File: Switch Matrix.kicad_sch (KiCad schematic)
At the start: 131 parts, among them SW1 SD_6B1D, SW10 SD_4B1E, SW100 SD_4B3E, SW101 SD_4B3E, SW102 SD_4B3E, SW103 SD_4B3E, SW104 SD_4B3E, SW105 SD_4B3E, SW106 SD_4B3E, SW107 SD_4B3E, SW108 SD_4B3E, SW109 SD_4B3E, SW11 SD_4B1E, SW110 SD_4B3E, SW111 SD_4B3E, SW112 SD_6B1D, SW113 SD_4B3E, SW114 SD_4B3E, SW115 UNPOPULATED, SW116 SD_4B3E, SW117 SD_5B3E, SW118 SD_4B3E, SW119 UNPOPULATED, SW12 SD_6B1D, SW120 SD_4B3E, SW121 SD_4B3E, SW122 SD_4B3E, SW122a0 UNPOPULATED, SW123 SD_4B3E, SW123a0 UNPOPULATED, SW124 UNPOPULATED, SW124a0 SD_4B3E, SW125 SD_4B3E, SW126 SD_4B3E, SW127 UNPOPULATED, SW128 SD_4B3E, SW13 SD_4B1E, SW14 SD_6B1D, SW15 SD_4B1E, SW16 SD_6B1D, SW17 SD_4B1E, SW18 SD_6B1D, SW19 SD_4B1E, SW2 SD_4B1E, SW20 SD_6B1D, SW21 SD_4B1E, SW22 SD_6B1D, SW23 SD_4B1E, SW24 SD_6B1D, SW25 SD_4B3E, SW26 SD_4B3E, SW27 SD_6B1D, SW28 SD_4B3E, SW29 SD_4B3E, SW3 SD_6B1D, SW30 SD_4B3E, SW31 SD_4B3E, SW32 SD_4B3E, SW33 SD_4B3E, SW34 SD_4B3E, SW35 SD_4B3E, SW36 SD_4B3E, SW37 SD_4B3E, SW38 SD_4B3E, SW39 SD_4B3E, SW4 SD_4B1E, SW40 SD_4B3E, SW41 UNPOPULATED, SW42 SD_4B3E, SW43 SD_4B3E, SW44 SD_4B3E, SW45 SD_4B3E, SW46 SD_6B1D, SW47 SD_4B3E, SW48 SD_4B3E, SW49 SD_4B3E, SW5 SD_6B1D, SW50 SD_4B3E, SW51 SD_4B3E, SW52 SD_6B1D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

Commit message: wip: remove +5v line
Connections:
- removed net +5V: SW1.2 (+5V), SW10.2 (+5V), SW100.2 (+5V), SW101.2 (+5V), SW102.2 (+5V), SW103.2 (+5V), SW104.2 (+5V), SW105.2 (+5V), SW106.2 (+5V), SW107.2 (+5V), SW108.2 (+5V), SW109.2 (+5V), SW11.2 (+5V), SW110.2 (+5V), SW111.2 (+5V), SW112.2 (+5V), SW113.2 (+5V), SW114.2 (+5V), SW115.2 (+5V), SW116.2 (+5V), SW117.2 (+5V), SW118.2 (+5V), SW119.2 (+5V), SW12.2 (+5V), SW120.2 (+5V), SW121.2 (+5V), SW122.2 (+5V), SW122a0.2 (+5V), SW123.2 (+5V), SW123a0.2 (+5V), SW124.2 (+5V), SW124a0.2 (+5V), SW125.2 (+5V), SW126.2 (+5V), SW127.2 (+5V), SW128.2 (+5V), SW13.2 (+5V), SW14.2 (+5V), SW15.2 (+5V), SW16.2 (+5V), SW17.2 (+5V), SW18.2 (+5V), SW19.2 (+5V), SW2.2 (+5V), SW20.2 (+5V), SW21.2 (+5V), SW22.2 (+5V), SW23.2 (+5V), SW24.2 (+5V), SW25.2 (+5V), SW26.2 (+5V), SW27.2 (+5V), SW28.2 (+5V), SW29.2 (+5V), SW3.2 (+5V), SW30.2 (+5V), SW31.2 (+5V), SW32.2 (+5V), SW33.2 (+5V), SW34.2 (+5V), SW35.2 (+5V), SW36.2 (+5V), SW37.2 (+5V), SW38.2 (+5V), SW39.2 (+5V), SW4.2 (+5V), SW40.2 (+5V), SW41.2 (+5V), SW42.2 (+5V), SW43.2 (+5V), SW44.2 (+5V), SW45.2 (+5V), SW46.2 (+5V), SW47.2 (+5V), SW48.2 (+5V), SW49.2 (+5V), SW5.2 (+5V), SW50.2 (+5V), SW51.2 (+5V), SW52.2 (+5V), SW53.2 (+5V), SW54.2 (+5V), SW55.2 (+5V), SW56.2 (+5V), SW57.2 (+5V), SW58.2 (+5V), SW59.2 (+5V), SW6.2 (+5V), SW60.2 (+5V), SW61.2 (+5V), SW62.2 (+5V), SW63.2 (+5V), SW64.2 (+5V), SW65.2 (+5V), SW66.2 (+5V), SW67.2 (+5V), SW68.2 (+5V), SW69.2 (+5V), SW7.2 (+5V), SW70.2 (+5V), SW71.2 (+5V), SW72.2 (+5V), SW73.2 (+5V), SW74.2 (+5V), SW75.2 (+5V), SW76.2 (+5V), SW77.2 (+5V), SW78.2 (+5V), SW79.2 (+5V), SW8.2 (+5V), SW80.2 (+5V), SW81.2 (+5V), SW82.2 (+5V), SW83.2 (+5V), SW84.2 (+5V), SW85.2 (+5V), SW86.2 (+5V), SW87.2 (+5V), SW88.2 (+5V), SW89.2 (+5V), SW9.2 (+5V), SW90.2 (+5V), SW91.2 (+5V), SW92.2 (+5V), SW93.2 (+5V), SW94.2 (+5V), SW95.2 (+5V), SW96.2 (+5V), SW97.2 (+5V), SW98.2 (+5V), SW99.2 (+5V)

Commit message: wip: footprint and symbols update 1
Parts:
- SW1, SW10, SW100, SW101, SW102, SW103, SW104, SW105, SW106, SW107, SW108, SW109, SW11, SW110, SW111, SW112, SW113, SW114, SW115, SW116, SW117, SW118, SW119, SW12, SW120, SW121, SW122, SW122a0, SW123, SW123a0, SW124, SW124a0, SW125, SW126, SW127, SW128, SW13, SW14, SW15, SW16, SW17, SW18, SW19, SW2, SW20, SW21, SW22, SW23, SW24, SW25, SW26, SW27, SW28, SW29, SW3, SW30, SW31, SW32, SW33, SW34, SW35, SW36, SW37, SW38, SW39, SW4, SW40, SW41, SW42, SW43, SW44, SW45, SW46, SW47, SW48, SW49, SW5, SW50, SW51, SW52, SW53, SW54, SW55, SW56, SW57, SW58, SW59, SW6, SW60, SW61, SW62, SW63, SW64, SW65, SW66, SW67, SW68, SW69, SW7, SW70, SW71, SW72, SW73, SW74, SW75, SW76, SW77, SW78, SW79, SW8, SW80, SW81, SW82, SW83, SW84, SW85, SW86, SW87, SW88, SW89, SW9, SW90, SW91, SW92, SW93, SW94, SW95, SW96, SW97, SW98, SW99: symbol MicroSwitch_SD_4B3E:SD_4B3E -> MicroSwitch:MicroSwitchSDSeriesE

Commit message: pcb diode 1,2 row placement
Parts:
- added D1, D10, D100, D101, D102, D103, D104, D105, D106, D107, D108, D109, D11, D110, D111, D112, D113, D114, D115, D116, D117, D118, D119, D12, D120, D122, D123, D124, D125, D126, D127, D128, D13, D14, D15, D16, D17, D18, D19, D2, D20, D21, D22, D23, D24, D25, D26, D27, D28, D29, D3, D30, D31, D32, D33, D34, D35, D36, D37, D38, D39, D4, D40, D41, D42, D43, D44, D45, D46, D47, D48, D49, D5, D50, D51, D52, D53, D54, D55, D56, D57, D58, D59, D6, D60, D61, D62, D63, D64, D65, D66, D67, D68, D69, D7, D70, D71, D72, D73, D74, D75, D76, D77, D78, D79, D8, D80, D81, D82, D83, D84, D85, D86, D87, D88, D89, D9, D90, D91, D92, D93, D94, D95, D96, D97, D98, D99, D`1`17: D, Diode_THT:D_A-405_P7.62mm_Horizontal, symbol Device:D
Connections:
- net COL0: now also SW120.1 (in), SW22.1 (in), SW26.1 (in), SW3.1 (in), SW46.1 (in), SW50.1 (in), SW73.1 (in), SW97.1 (in); no longer SW120.3 (VOUT), SW22.3 (VOUT), SW26.3 (VOUT), SW3.3 (VOUT), SW46.3 (VOUT), SW50.3 (VOUT), SW73.3 (VOUT), SW97.3 (VOUT)
- net COL1: now also SW119.1 (in), SW2.1 (in), SW23.1 (in), SW25.1 (in), SW47.1 (in), SW49.1 (in), SW72.1 (in), SW96.1 (in); no longer SW119.3 (VOUT), SW2.3 (VOUT), SW23.3 (VOUT), SW25.3 (VOUT), SW47.3 (VOUT), SW49.3 (VOUT), SW72.3 (VOUT), SW96.3 (VOUT)
- net COL10: now also SW106.1 (in), SW11.1 (in), SW115.1 (in), SW35.1 (in), SW59.1 (in), SW69.1 (in), SW82.1 (in), SW92.1 (in); no longer SW106.3 (VOUT), SW11.3 (VOUT), SW115.3 (VOUT), SW35.3 (VOUT), SW59.3 (VOUT), SW69.3 (VOUT), SW82.3 (VOUT), SW92.3 (VOUT)
- net COL11: now also SW107.1 (in), SW114.1 (in), SW12.1 (in), SW36.1 (in), SW60.1 (in), SW68.1 (in), SW83.1 (in), SW91.1 (in); no longer SW107.3 (VOUT), SW114.3 (VOUT), SW12.3 (VOUT), SW36.3 (VOUT), SW60.3 (VOUT), SW68.3 (VOUT), SW83.3 (VOUT), SW91.3 (VOUT)
- net COL12: now also SW108.1 (in), SW113.1 (in), SW13.1 (in), SW37.1 (in), SW61.1 (in), SW67.1 (in), SW84.1 (in), SW90.1 (in); no longer SW108.3 (VOUT), SW113.3 (VOUT), SW13.3 (VOUT), SW37.3 (VOUT), SW61.3 (VOUT), SW67.3 (VOUT), SW84.3 (VOUT), SW90.3 (VOUT)
- net COL13: now also SW123.1 (in), SW123a0.1 (in), SW127.1 (in), SW16.1 (in), SW40.1 (in), SW64.1 (in), SW65.1 (in), SW87.1 (in), SW88.1 (in); no longer SW123.3 (VOUT), SW123a0.3 (VOUT), SW127.3 (VOUT), SW16.3 (VOUT), SW40.3 (VOUT), SW64.3 (VOUT), SW65.3 (VOUT), SW87.3 (VOUT), SW88.3 (VOUT)
- net COL14: now also SW109.1 (in), SW112.1 (in), SW14.1 (in), SW38.1 (in), SW62.1 (in), SW66.1 (in), SW85.1 (in), SW89.1 (in); no longer SW109.3 (VOUT), SW112.3 (VOUT), SW14.3 (VOUT), SW38.3 (VOUT), SW62.3 (VOUT), SW66.3 (VOUT), SW85.3 (VOUT), SW89.3 (VOUT)
- net COL15: now also SW110.1 (in), SW128.1 (in), SW15.1 (in), SW24.1 (in), SW39.1 (in), SW48.1 (in), SW63.1 (in), SW86.1 (in); no longer SW110.3 (VOUT), SW128.3 (VOUT), SW15.3 (VOUT), SW24.3 (VOUT), SW39.3 (VOUT), SW48.3 (VOUT), SW63.3 (VOUT), SW86.3 (VOUT)
- net COL2: now also SW121.1 (in), SW21.1 (in), SW27.1 (in), SW4.1 (in), SW45.1 (in), SW51.1 (in), SW74.1 (in), SW98.1 (in); no longer SW121.3 (VOUT), SW21.3 (VOUT), SW27.3 (VOUT), SW4.3 (VOUT), SW45.3 (VOUT), SW51.3 (VOUT), SW74.3 (VOUT), SW98.3 (VOUT)
- net COL3: now also SW118.1 (in), SW20.1 (in), SW28.1 (in), SW44.1 (in), SW5.1 (in), SW52.1 (in), SW75.1 (in), SW99.1 (in); no longer SW118.3 (VOUT), SW20.3 (VOUT), SW28.3 (VOUT), SW44.3 (VOUT), SW5.3 (VOUT), SW52.3 (VOUT), SW75.3 (VOUT), SW99.3 (VOUT)
- net COL4: now also SW1.1 (in), SW100.1 (in), SW111.1 (in), SW122.1 (in), SW122a0.1 (in), SW124.1 (in), SW124a0.1 (in), SW29.1 (in), SW53.1 (in), SW76.1 (in); no longer SW1.3 (VOUT), SW100.3 (VOUT), SW111.3 (VOUT), SW122.3 (VOUT), SW122a0.3 (VOUT), SW124.3 (VOUT), SW124a0.3 (VOUT), SW29.3 (VOUT), SW53.3 (VOUT), SW76.3 (VOUT)
- net COL5: now also SW101.1 (in), SW18.1 (in), SW30.1 (in), SW42.1 (in), SW54.1 (in), SW6.1 (in), SW77.1 (in), SW95.1 (in); no longer SW101.3 (VOUT), SW18.3 (VOUT), SW30.3 (VOUT), SW42.3 (VOUT), SW54.3 (VOUT), SW6.3 (VOUT), SW77.3 (VOUT), SW95.3 (VOUT)
- net COL6: now also SW102.1 (in), SW126.1 (in), SW17.1 (in), SW31.1 (in), SW41.1 (in), SW55.1 (in), SW7.1 (in), SW78.1 (in); no longer SW102.3 (VOUT), SW126.3 (VOUT), SW17.3 (VOUT), SW31.3 (VOUT), SW41.3 (VOUT), SW55.3 (VOUT), SW7.3 (VOUT), SW78.3 (VOUT)
- net COL7: now also SW103.1 (in), SW125.1 (in), SW19.1 (in), SW32.1 (in), SW43.1 (in), SW56.1 (in), SW79.1 (in), SW8.1 (in); no longer SW103.3 (VOUT), SW125.3 (VOUT), SW19.3 (VOUT), SW32.3 (VOUT), SW43.3 (VOUT), SW56.3 (VOUT), SW79.3 (VOUT), SW8.3 (VOUT)
- net COL8: now also SW104.1 (in), SW117.1 (in), SW33.1 (in), SW57.1 (in), SW71.1 (in), SW80.1 (in), SW9.1 (in), SW94.1 (in); no longer SW104.3 (VOUT), SW117.3 (VOUT), SW33.3 (VOUT), SW57.3 (VOUT), SW71.3 (VOUT), SW80.3 (VOUT), SW9.3 (VOUT), SW94.3 (VOUT)
- net COL9: now also SW10.1 (in), SW105.1 (in), SW116.1 (in), SW34.1 (in), SW58.1 (in), SW70.1 (in), SW81.1 (in), SW93.1 (in); no longer SW10.3 (VOUT), SW105.3 (VOUT), SW116.3 (VOUT), SW34.3 (VOUT), SW58.3 (VOUT), SW70.3 (VOUT), SW81.3 (VOUT), SW93.3 (VOUT)
- net ROW0: now also SW122a0.2 (out); no longer SW10.1 (VCC), SW11.1 (VCC), SW12.1 (VCC), SW122.1 (VCC), SW122a0.1 (VCC), SW13.1 (VCC), SW14.1 (VCC), SW15.1 (VCC), SW16.1 (VCC), SW2.1 (VCC), SW3.1 (VCC), SW4.1 (VCC), SW5.1 (VCC), SW6.1 (VCC), SW7.1 (VCC), SW8.1 (VCC), SW9.1 (VCC)
- net ROW1: now also D25.1 (K), D26.1 (K), D27.1 (K), D28.1 (K), D29.1 (K), D30.1 (K), D31.1 (K), D32.1 (K), D33.1 (K), D34.1 (K), D35.1 (K), D36.1 (K), D37.1 (K), D38.1 (K), D39.1 (K), D40.1 (K); no longer SW25.1 (VCC), SW26.1 (VCC), SW27.1 (VCC), SW28.1 (VCC), SW29.1 (VCC), SW30.1 (VCC), SW31.1 (VCC), SW32.1 (VCC), SW33.1 (VCC), SW34.1 (VCC), SW35.1 (VCC), SW36.1 (VCC), SW37.1 (VCC), SW38.1 (VCC), SW39.1 (VCC), SW40.1 (VCC)
- net ROW2: now also D49.1 (K), D50.1 (K), D51.1 (K), D52.1 (K), D53.1 (K), D54.1 (K), D55.1 (K), D56.1 (K); no longer SW49.1 (VCC), SW50.1 (VCC), SW51.1 (VCC), SW52.1 (VCC), SW53.1 (VCC), SW54.1 (VCC), SW55.1 (VCC), SW56.1 (VCC), SW57.1 (VCC), SW58.1 (VCC), SW59.1 (VCC), SW60.1 (VCC), SW61.1 (VCC), SW62.1 (VCC), SW63.1 (VCC), SW64.1 (VCC)
- net ROW3: now also D72.1 (K), D73.1 (K), D74.1 (K), D75.1 (K), D76.1 (K), D77.1 (K), D78.1 (K), D79.1 (K); no longer SW72.1 (VCC), SW73.1 (VCC), SW74.1 (VCC), SW75.1 (VCC), SW76.1 (VCC), SW77.1 (VCC), SW78.1 (VCC), SW79.1 (VCC), SW80.1 (VCC), SW81.1 (VCC), SW82.1 (VCC), SW83.1 (VCC), SW84.1 (VCC), SW85.1 (VCC), SW86.1 (VCC), SW87.1 (VCC)
- net ROW4: now also SW123a0.2 (out), D100.1 (K), D101.1 (K), D102.1 (K), D103.1 (K), D96.1 (K), D97.1 (K), D98.1 (K), D99.1 (K); no longer SW100.1 (VCC), SW101.1 (VCC), SW102.1 (VCC), SW103.1 (VCC), SW104.1 (VCC), SW105.1 (VCC), SW106.1 (VCC), SW107.1 (VCC), SW108.1 (VCC), SW109.1 (VCC), SW110.1 (VCC), SW123.1 (VCC), SW123a0.1 (VCC), SW96.1 (VCC), SW97.1 (VCC), SW98.1 (VCC), SW99.1 (VCC)
- net ROW5: now also D111.1 (K), D118.1 (K), D119.1 (K), D120.1 (K), D125.1 (K), D126.1 (K), D95.1 (K), D`1`17.1 (K); no longer SW111.1 (VCC), SW112.1 (VCC), SW113.1 (VCC), SW114.1 (VCC), SW115.1 (VCC), SW116.1 (VCC), SW117.1 (VCC), SW118.1 (VCC), SW119.1 (VCC), SW120.1 (VCC), SW121.1 (VCC), SW125.1 (VCC), SW126.1 (VCC), SW127.1 (VCC), SW128.1 (VCC), SW95.1 (VCC)
- net ROW6: now also SW124a0.2 (out), D1.1 (K), D124.1 (K), D17.1 (K), D18.1 (K), D19.1 (K), D20.1 (K), D21.1 (K), D22.1 (K), D23.1 (K), D41.1 (K), D42.1 (K), D43.1 (K), D44.1 (K), D45.1 (K), D46.1 (K), D47.1 (K); no longer SW124.1 (VCC), SW124a0.1 (VCC), SW41.1 (VCC), SW42.1 (VCC), SW43.1 (VCC), SW44.1 (VCC), SW45.1 (VCC), SW46.1 (VCC), SW47.1 (VCC), SW48.1 (VCC), SW88.1 (VCC), SW89.1 (VCC), SW90.1 (VCC), SW91.1 (VCC), SW92.1 (VCC), SW93.1 (VCC), SW94.1 (VCC)
- removed net ROW7: SW1.1 (VCC), SW17.1 (VCC), SW18.1 (VCC), SW19.1 (VCC), SW20.1 (VCC), SW21.1 (VCC), SW22.1 (VCC), SW23.1 (VCC), SW24.1 (VCC), SW65.1 (VCC), SW66.1 (VCC), SW67.1 (VCC), SW68.1 (VCC), SW69.1 (VCC), SW70.1 (VCC), SW71.1 (VCC)
- new net: D80.1 (K), D81.1 (K), D82.1 (K), D83.1 (K), D84.1 (K), D85.1 (K), D86.1 (K), D87.1 (K)
- new net: D85.2 (A), SW85.2 (out)
- new net: D48.2 (A), SW48.2 (out)
- new net: D41.2 (A), SW41.2 (out)
- new net: D123.2 (A), SW123.2 (out)
- new net: D4.2 (A), SW4.2 (out)
- new net: D57.1 (K), D58.1 (K), D59.1 (K), D60.1 (K), D61.1 (K), D62.1 (K), D63.1 (K), D64.1 (K)
- new net: D58.2 (A), SW58.2 (out)
- new net: D104.1 (K), D105.1 (K), D106.1 (K), D107.1 (K), D108.1 (K), D109.1 (K), D110.1 (K), D123.1 (K)
- new net: D109.2 (A), SW109.2 (out)
- new net: D119.2 (A), SW119.2 (out)
- new net: D11.2 (A), SW11.2 (out)
- new net: D21.2 (A), SW21.2 (out)
- new net: D29.2 (A), SW29.2 (out)
- new net: D24.1 (K), D65.1 (K), D66.1 (K), D67.1 (K), D68.1 (K), D69.1 (K), D70.1 (K), D71.1 (K)
- new net: D68.2 (A), SW68.2 (out)
- new net: D18.2 (A), SW18.2 (out)
- new net: D98.2 (A), SW98.2 (out)
- new net: D90.2 (A), SW90.2 (out)
- new net: D89.2 (A), SW89.2 (out)
- new net: D84.2 (A), SW84.2 (out)
- new net: D112.1 (K), D113.1 (K), D114.1 (K), D115.1 (K), D116.1 (K), D117.1 (K), D127.1 (K), D128.1 (K)
- new net: D114.2 (A), SW114.2 (out)
- new net: D117.2 (A), SW117.2 (out)
- new net: D36.2 (A), SW36.2 (out)
- new net: D111.2 (A), SW111.2 (out)
- new net: D10.1 (K), D11.1 (K), D122.1 (K), D2.1 (K), D3.1 (K), D4.1 (K), D5.1 (K), D6.1 (K), D7.1 (K), D8.1 (K), D9.1 (K)
- new net: D3.2 (A), SW3.2 (out)
- new net: D124.2 (A), SW124.2 (out)
- new net: D106.2 (A), SW106.2 (out)
- new net: D120.2 (A), SW120.2 (out)
- new net: D70.2 (A), SW70.2 (out)
- new net: D80.2 (A), SW80.2 (out)
- new net: D128.2 (A), SW128.2 (out)
- new net: D45.2 (A), SW45.2 (out)
- new net: D97.2 (A), SW97.2 (out)
- new net: D107.2 (A), SW107.2 (out)
- new net: D15.2 (A), SW15.2 (out)
- new net: D71.2 (A), SW71.2 (out)
- new net: D118.2 (A), SW118.2 (out)
- new net: D108.2 (A), SW108.2 (out)
- new net: D99.2 (A), SW99.2 (out)
- new net: D51.2 (A), SW51.2 (out)
- new net: D1.2 (A), SW1.2 (out)
- new net: D83.2 (A), SW83.2 (out)
- new net: D86.2 (A), SW86.2 (out)
- new net: D12.1 (K), D13.1 (K), D14.1 (K), D15.1 (K), D16.1 (K)
- new net: D52.2 (A), SW52.2 (out)
- new net: D110.2 (A), SW110.2 (out)
- new net: D66.2 (A), SW66.2 (out)
- new net: D77.2 (A), SW77.2 (out)
- new net: D59.2 (A), SW59.2 (out)
- new net: D54.2 (A), SW54.2 (out)
- new net: D6.2 (A), SW6.2 (out)
- new net: D24.2 (A), SW24.2 (out)
- new net: D43.2 (A), SW43.2 (out)
- new net: D47.2 (A), SW47.2 (out)
- new net: D61.2 (A), SW61.2 (out)
- new net: D96.2 (A), SW96.2 (out)
- new net: D63.2 (A), SW63.2 (out)
- new net: D125.2 (A), SW125.2 (out)
- new net: D46.2 (A), SW46.2 (out)
- new net: D32.2 (A), SW32.2 (out)
- new net: D53.2 (A), SW53.2 (out)
- new net: D34.2 (A), SW34.2 (out)
- new net: D39.2 (A), SW39.2 (out)
- new net: D79.2 (A), SW79.2 (out)
- new net: D115.2 (A), SW115.2 (out)
- new net: D102.2 (A), SW102.2 (out)
- new net: D9.2 (A), SW9.2 (out)
- new net: D5.2 (A), SW5.2 (out)
- new net: D94.2 (A), SW94.2 (out)
- new net: D26.2 (A), SW26.2 (out)
- new net: D104.2 (A), SW104.2 (out)
- new net: D69.2 (A), SW69.2 (out)
- new net: D73.2 (A), SW73.2 (out)
- new net: D22.2 (A), SW22.2 (out)
- new net: D95.2 (A), SW95.2 (out)
- new net: D48.1 (K), D88.1 (K), D89.1 (K), D90.1 (K), D91.1 (K), D92.1 (K), D93.1 (K), D94.1 (K)
- new net: D57.2 (A), SW57.2 (out)
- new net: D40.2 (A), SW40.2 (out)
- new net: D72.2 (A), SW72.2 (out)
- new net: D65.2 (A), SW65.2 (out)
- new net: D81.2 (A), SW81.2 (out)
- new net: D64.2 (A), SW64.2 (out)
- new net: D100.2 (A), SW100.2 (out)
- new net: D28.2 (A), SW28.2 (out)
- new net: D37.2 (A), SW37.2 (out)
- new net: D74.2 (A), SW74.2 (out)
- new net: D60.2 (A), SW60.2 (out)
- new net: D103.2 (A), SW103.2 (out)
- new net: D10.2 (A), SW10.2 (out)
- new net: D105.2 (A), SW105.2 (out)
- new net: D56.2 (A), SW56.2 (out)
- new net: D75.2 (A), SW75.2 (out)
- new net: D88.2 (A), SW88.2 (out)
- new net: D67.2 (A), SW67.2 (out)
- new net: D122.2 (A), SW122.2 (out)
- new net: D19.2 (A), SW19.2 (out)
- new net: D101.2 (A), SW101.2 (out)
- new net: D50.2 (A), SW50.2 (out)
- new net: D112.2 (A), SW112.2 (out)
- new net: D13.2 (A), SW13.2 (out)
- new net: D87.2 (A), SW87.2 (out)
- new net: D44.2 (A), SW44.2 (out)
- new net: D27.2 (A), SW27.2 (out)
- new net: D127.2 (A), SW127.2 (out)
- new net: D62.2 (A), SW62.2 (out)
- new net: D38.2 (A), SW38.2 (out)
- new net: D116.2 (A), SW116.2 (out)
- new net: D31.2 (A), SW31.2 (out)
- new net: D16.2 (A), SW16.2 (out)
- new net: D82.2 (A), SW82.2 (out)
- new net: D55.2 (A), SW55.2 (out)
- new net: D30.2 (A), SW30.2 (out)
- new net: D`1`17.2 (A), SW121.2 (out)
- new net: D14.2 (A), SW14.2 (out)
- new net: D49.2 (A), SW49.2 (out)
- new net: D93.2 (A), SW93.2 (out)
- new net: D91.2 (A), SW91.2 (out)
- new net: D78.2 (A), SW78.2 (out)
- new net: D76.2 (A), SW76.2 (out)
- new net: D113.2 (A), SW113.2 (out)
- new net: D7.2 (A), SW7.2 (out)
- new net: D33.2 (A), SW33.2 (out)
- new net: D42.2 (A), SW42.2 (out)
- new net: D12.2 (A), SW12.2 (out)
- new net: D23.2 (A), SW23.2 (out)
- new net: D35.2 (A), SW35.2 (out)
- new net: D92.2 (A), SW92.2 (out)
- new net: D17.2 (A), SW17.2 (out)
- new net: D25.2 (A), SW25.2 (out)
- new net: D8.2 (A), SW8.2 (out)
- new net: D126.2 (A), SW126.2 (out)
- new net: D2.2 (A), SW2.2 (out)
- new net: D20.2 (A), SW20.2 (out)
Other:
- moved on the sheet: SW1, SW10, SW100, SW101, SW102, SW103, SW104, SW105, SW106, SW107, SW108, SW109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

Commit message: wip: pcb tuning
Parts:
- D1, D10, D100, D101, D102, D103, D104, D105, D106, D107, D108, D109, D11, D110, D111, D112, D113, D114, D115, D116, D117, D118, D119, D12, D120, D122, D123, D124, D125, D126, D127, D128, D13, D14, D15, D16, D17, D18, D19, D2, D20, D21, D22, D23, D24, D25, D26, D27, D28, D29, D3, D30, D31, D32, D33, D34, D35, D36, D37, D38, D39, D4, D40, D41, D42, D43, D44, D45, D46, D47, D48, D49, D5, D50, D51, D52, D53, D54, D55, D56, D57, D58, D59, D6, D60, D61, D62, D63, D64, D65, D66, D67, D68, D69, D7, D70, D71, D72, D73, D74, D75, D76, D77, D78, D79, D8, D80, D81, D82, D83, D84, D85, D86, D87, D88, D89, D9, D90, D91, D92, D93, D94, D95, D96, D97, D98, D99, D`1`17: footprint Diode_THT:D_A-405_P7.62mm_Horizontal -> Diode_SMD:D_1210_3225Metric_Pad1.42x2.65mm_HandSolder

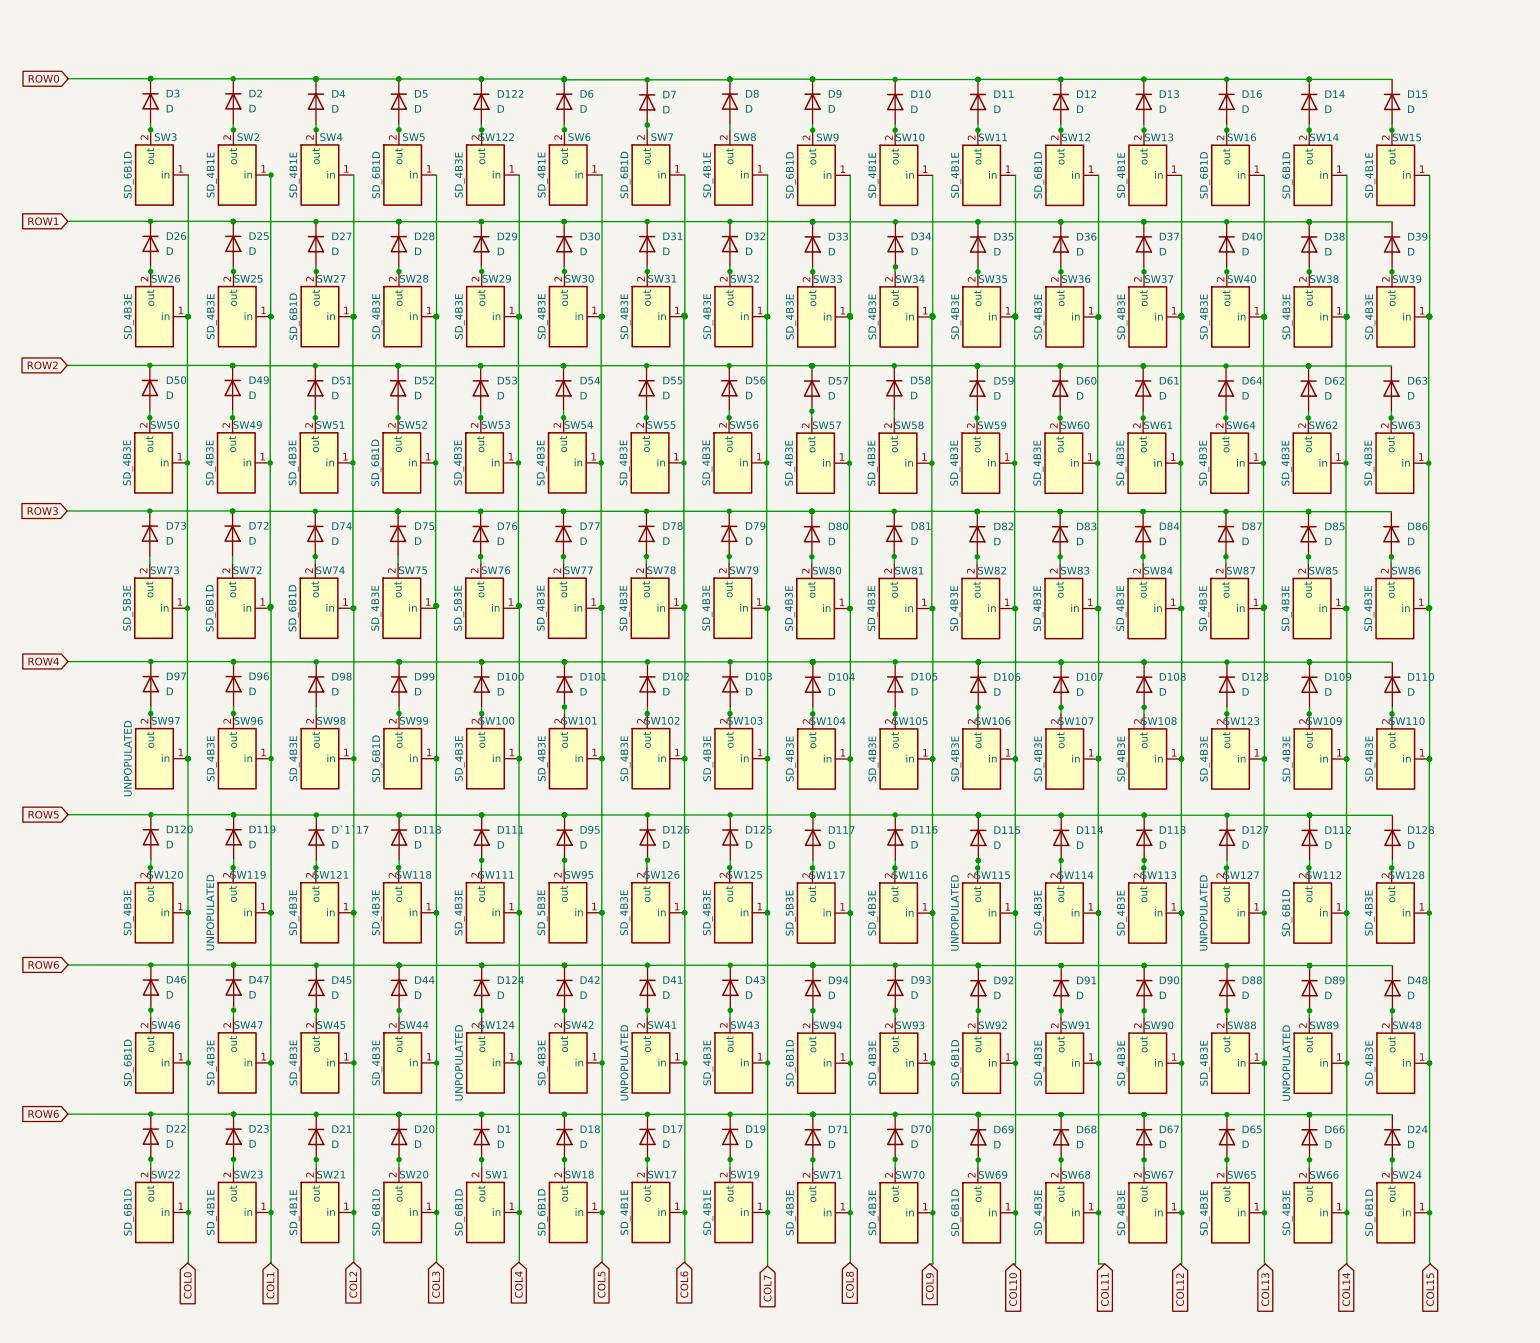
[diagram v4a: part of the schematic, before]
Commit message: wip: pcb tuning ROW2 and ROW3 with diodes
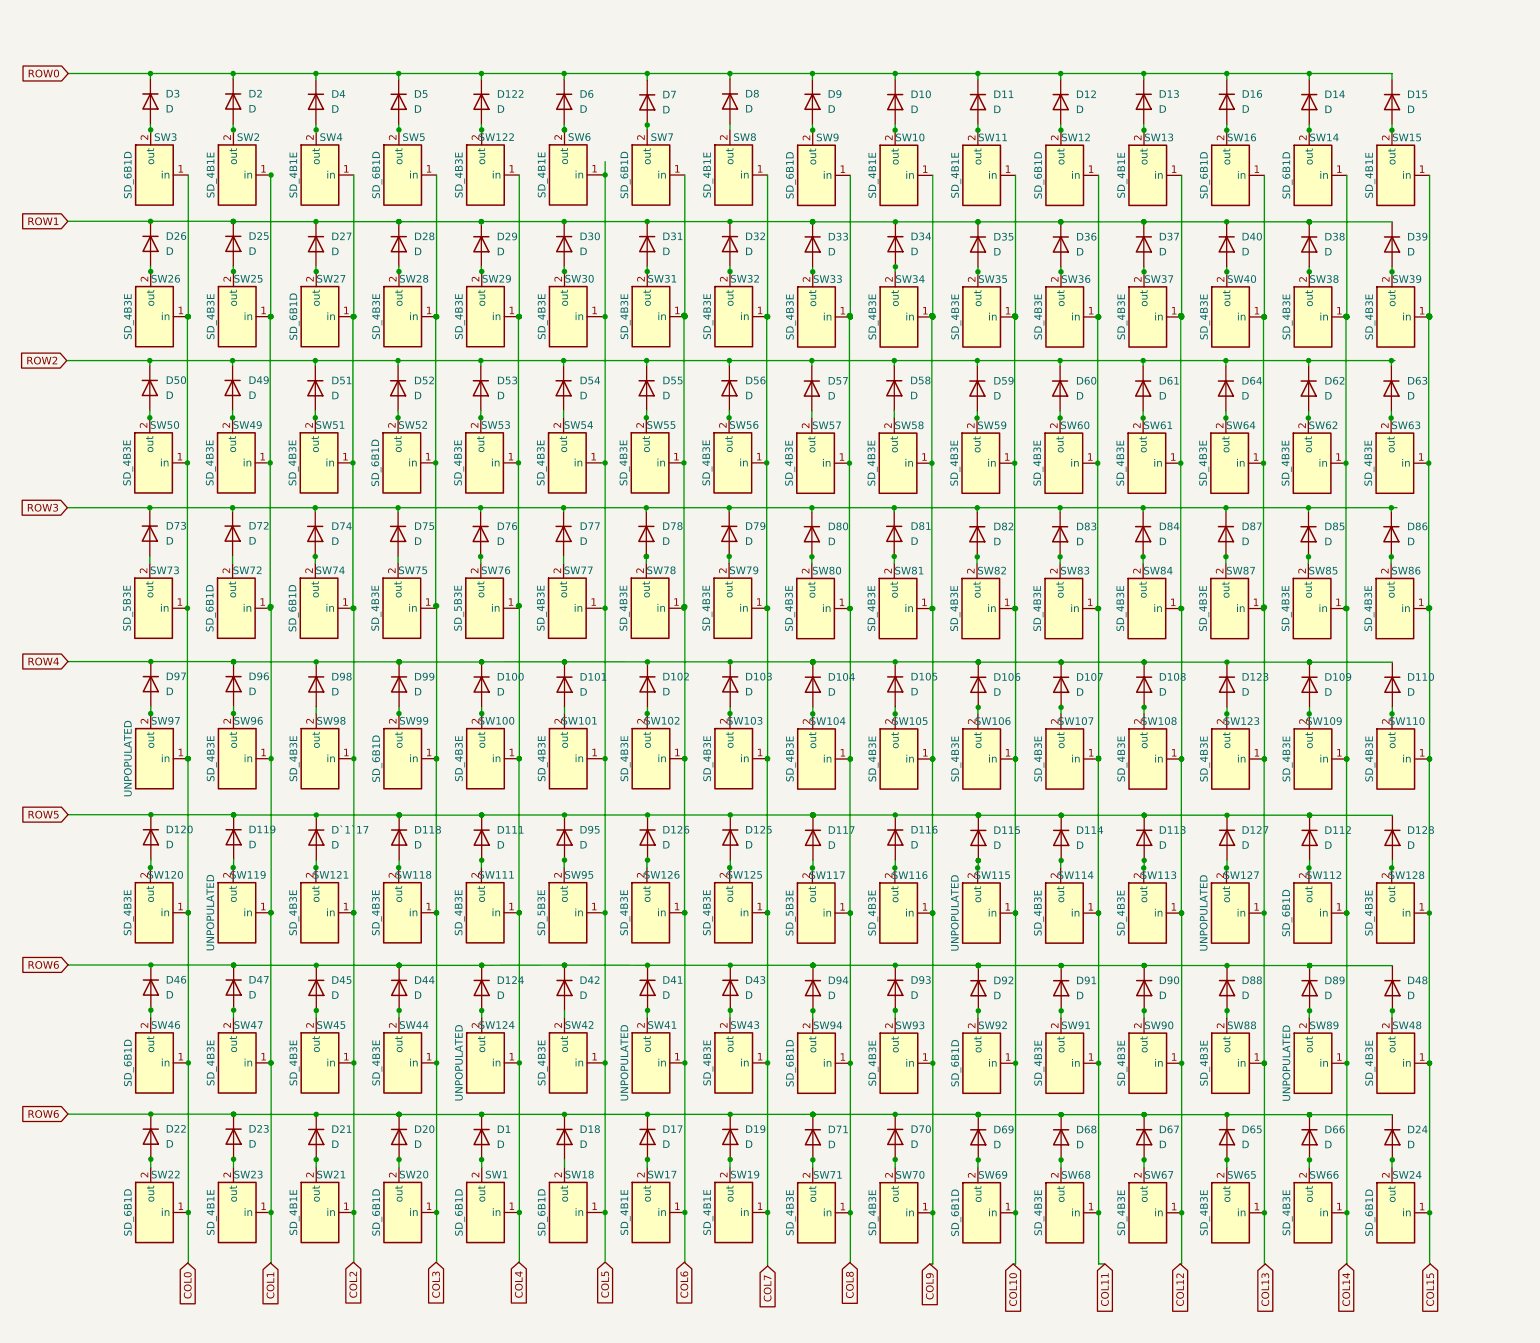
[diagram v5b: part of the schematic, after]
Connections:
- net ROW0: now also D10.1 (K), D11.1 (K), D12.1 (K), D122.1 (K), D13.1 (K), D14.1 (K), D15.1 (K), D16.1 (K), D2.1 (K), D3.1 (K), D4.1 (K), D5.1 (K), D6.1 (K), D7.1 (K), D8.1 (K), D9.1 (K)
- net ROW2: now also D57.1 (K), D58.1 (K), D59.1 (K), D60.1 (K), D61.1 (K), D62.1 (K), D63.1 (K), D64.1 (K)
- net ROW3: now also D80.1 (K), D81.1 (K), D82.1 (K), D83.1 (K), D84.1 (K), D85.1 (K), D86.1 (K), D87.1 (K)

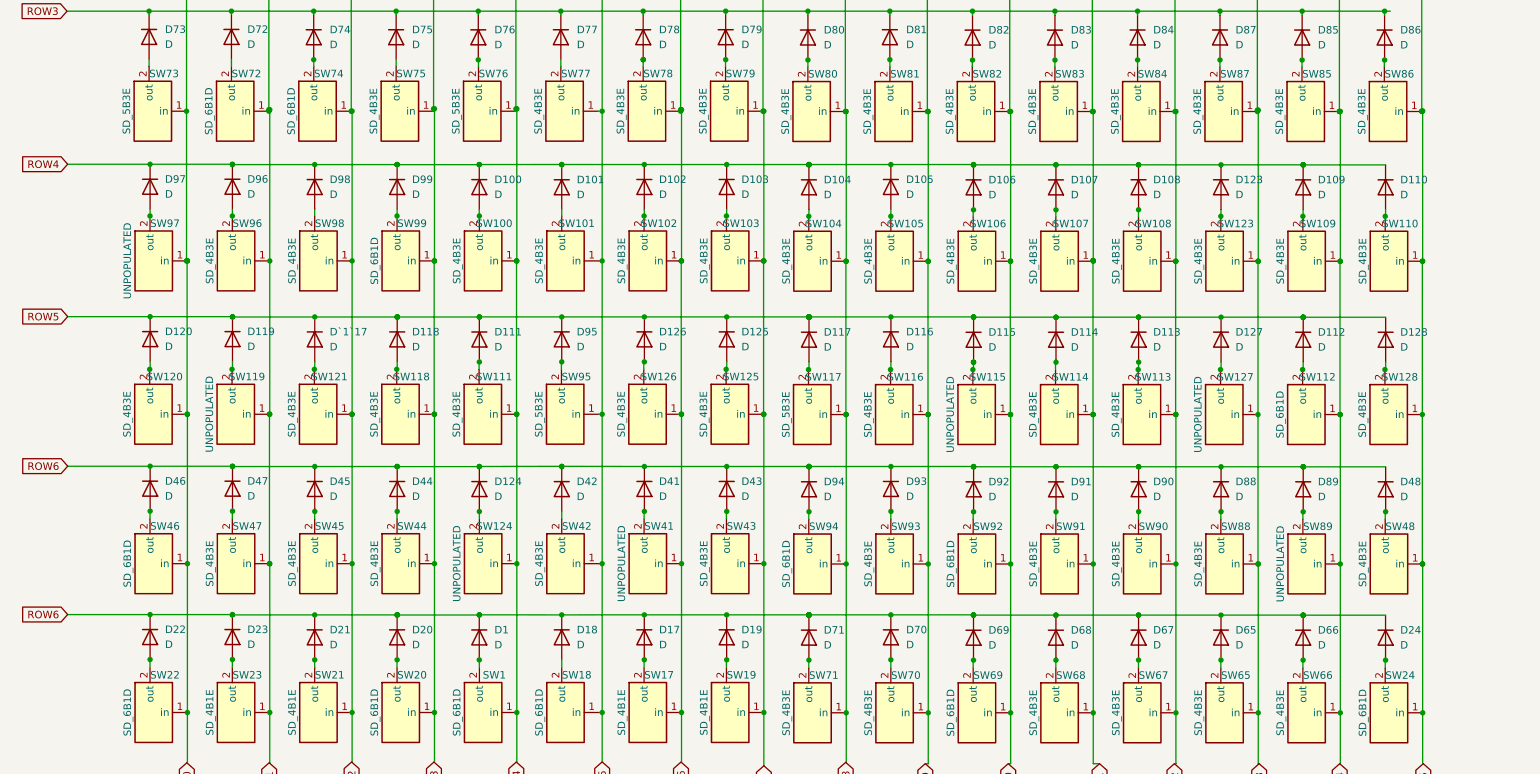
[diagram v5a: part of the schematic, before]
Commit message: wip: all D placed near SW, fixed Nets
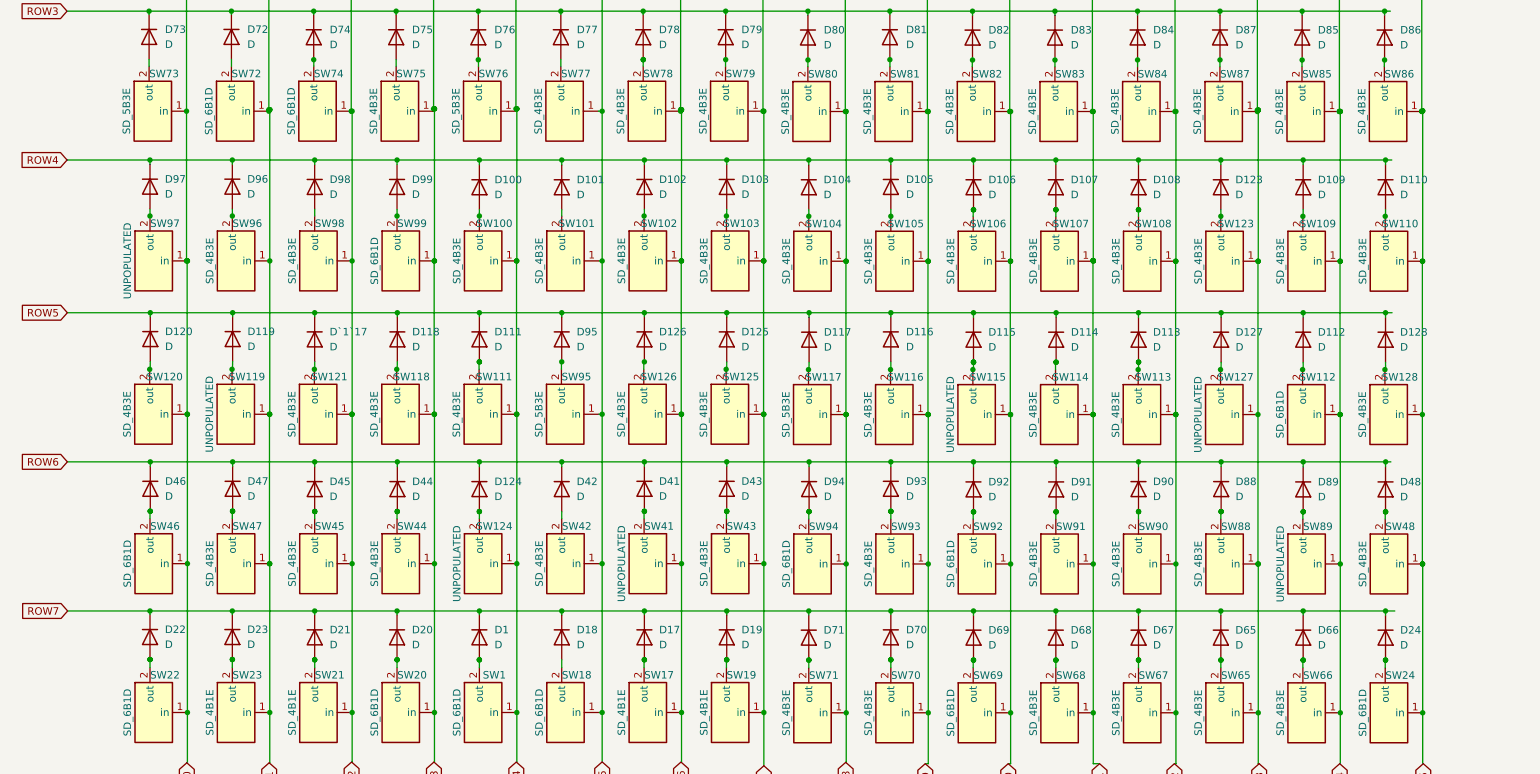
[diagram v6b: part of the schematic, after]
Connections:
- net ROW4: now also D104.1 (K), D105.1 (K), D106.1 (K), D107.1 (K), D108.1 (K), D109.1 (K), D110.1 (K), D123.1 (K)
- net ROW5: now also D112.1 (K), D113.1 (K), D114.1 (K), D115.1 (K), D116.1 (K), D117.1 (K), D127.1 (K), D128.1 (K)
- net ROW6: now also D48.1 (K), D88.1 (K), D89.1 (K), D90.1 (K), D91.1 (K), D92.1 (K), D93.1 (K), D94.1 (K); no longer D1.1 (K), D17.1 (K), D18.1 (K), D19.1 (K), D20.1 (K), D21.1 (K), D22.1 (K), D23.1 (K)
- net ROW7: now reaches D24.1 (K), D65.1 (K), D66.1 (K), D67.1 (K), D68.1 (K), D69.1 (K), D70.1 (K), D71.1 (K)
- net ROW7: now also D1.1 (K), D17.1 (K), D18.1 (K), D19.1 (K), D20.1 (K), D21.1 (K), D22.1 (K), D23.1 (K)
